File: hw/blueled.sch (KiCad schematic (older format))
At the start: 62 parts, among them J1 DC 5.5 - 42V, J2 LED Strip, J3 ICSP, J4 DC 5.5 - 42V, Q1 Q_PMOS_SDG, Q2 Q_PNP_EBC, Q3 BSS138, SW2 PUSH, U1 ATmega328P-AU, U2 HC-05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

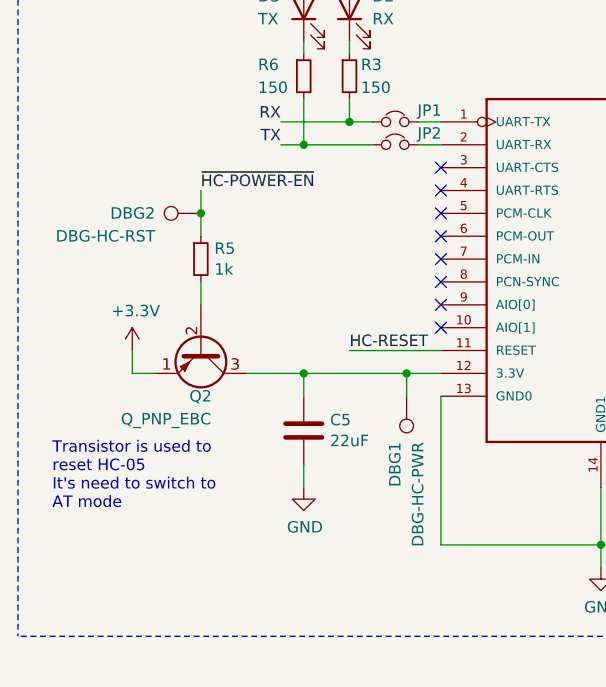
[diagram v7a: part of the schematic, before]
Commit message: fix(hw): change BJT to MOSFET to control HC-05 power
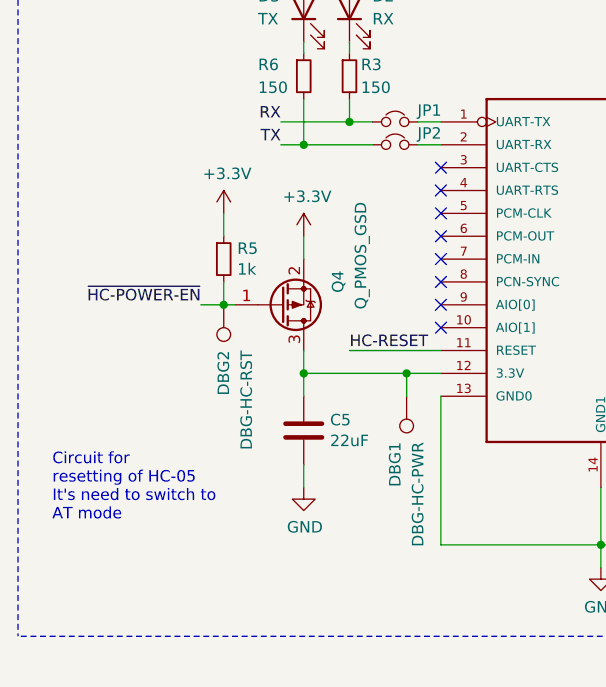
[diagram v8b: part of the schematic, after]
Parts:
- removed Q2: Q_PNP_EBC, Package_TO_SOT_SMD:SOT-323_SC-70_Handsoldering, symbol Device:Q_PNP_EBC
- added Q4: Q_PMOS_GSD, Package_TO_SOT_SMD:SOT-23, symbol Device:Q_PMOS_GSD
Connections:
- net +3V3: now also R5.1, Q4.2 (S)
- net ~HC-POWER-EN: now also R5.2, Q4.1 (G); no longer R5.1
- net at C5.1, DBG1.1, U2.12 (3.3V): now also Q4.3 (D)
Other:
- note added: "Circuit for\nresetting of HC-05\nIt's need to switch to \nAT mode"
- note removed: "Transistor is used to \nreset HC-05\nIt's need to switch to \nAT mode"
- moved on the sheet: DBG2, R5
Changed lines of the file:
@@
 Wire Wire Line
 	1850 5400 1850 5300
-Text Label 1400 4500 0    50   ~ 0
+Text Label 1400 5000 2    50   ~ 0
 ~HC-POWER-EN
 $Comp
 L Device:R_Small R5
 U 1 1 5E8E07EF
-P 1400 4800
-F 0 "R5" H 1459 4846 50  0000 L CNN
-F 1 "1k" H 1459 4755 50  0000 L CNN
-F 2 "Resistor_SMD:R_0805_2012Metric_Pad1.15x1.40mm_HandSolder" H 1400 4800 50  0001 C CNN
-F 3 "https://datasheet.lcsc.com/szlcsc/1810010118_YAGEO-RC0805FR-071KL_C95781.pdf" H 1400 4800 50  0001 C CNN
-F 4 "lcsc.com" H 1400 4800 50  0001 C CNN "Distributor"
-F 5 "RC0805FR-071KL" H 1400 4800 50  0001 C CNN "Manuf. Part"
-	1    1400 4800
-	1    0    0    -1
-$EndComp
-Wire Wire Line
-	1400 4500 1400 4600
-Wire Wire Line
-	1400 4900 1400 5000
-Wire Wire Line
-	1400 4600 1400 4700
-Connection ~ 1400 4600
+P 1500 4800
+F 0 "R5" H 1559 4846 50  0000 L CNN
+F 1 "1k" H 1559 4755 50  0000 L CNN
+F 2 "Resistor_SMD:R_0805_2012Metric_Pad1.15x1.40mm_HandSolder" H 1500 4800 50  0001 C CNN
+F 3 "https://datasheet.lcsc.com/szlcsc/1810010118_YAGEO-RC0805FR-071KL_C95781.pdf" H 1500 4800 50  0001 C CNN
+F 4 "lcsc.com" H 1500 4800 50  0001 C CNN "Distributor"
+F 5 "RC0805FR-071KL" H 1500 4800 50  0001 C CNN "Manuf. Part"
+	1    1500 4800
+	1    0    0    -1
+$EndComp
 $Comp
 L Connector:TestPoint DBG2
 U 1 1 5EAA6065
-P 1400 4600
-F 0 "DBG2" V 1400 4800 50  0000 L CNN
-F 1 "DBG-HC-RST" V 1300 4800 50  0000 L CNN
-F 2 "TestPoint:TestPoint_Pad_D1.0mm" H 1600 4600 50  0001 C CNN
-F 3 "~" H 1600 4600 50  0001 C CNN
-	1    1400 4600
-	0    -1   -1   0
-$EndComp
-$Comp
-L Device:Q_PNP_EBC Q2
-U 1 1 5E8AAEF6
-P 1400 5200
-F 0 "Q2" V 1600 5150 50  0000 L CNN
-F 1 "Q_PNP_EBC" V 1700 4850 50  0000 L CNN
-F 2 "Package_TO_SOT_SMD:SOT-323_SC-70_Handsoldering" H 1600 5300 50  0001 C CNN
-F 3 "https://datasheet.lcsc.com/szlcsc/1808280000_ROHM-Semicon-UMT2907A_C122972.pdf" H 1400 5200 50  0001 C CNN
-F 4 "lcsc.com" H 1400 5200 50  0001 C CNN "Distributor"
-F 5 "UMT2907A" H 1400 5200 50  0001 C CNN "Manuf. Part"
-	1    1400 5200
-	0    1    1    0
-$EndComp
-Wire Wire Line
-	1100 5300 1100 5200
-$Comp
-L power:+3.3V #PWR02
-U 1 1 5EB1E141
-P 1100 5200
-F 0 "#PWR02" H 1100 5050 50  0001 C CNN
-F 1 "+3.3V" H 1115 5373 50  0000 C CNN
-F 2 "" H 1100 5200 50  0001 C CNN
-F 3 "" H 1100 5200 50  0001 C CNN
-	1    1100 5200
-	1    0    0    -1
-$EndComp
-Wire Wire Line
-	1100 5300 1200 5300
-Wire Wire Line
-	1600 5300 1850 5300
+P 1500 5000
+F 0 "DBG2" V 1500 5200 50  0000 L CNN
+F 1 "DBG-HC-RST" V 1400 5200 50  0000 L CNN
+F 2 "TestPoint:TestPoint_Pad_D1.0mm" H 1700 5000 50  0001 C CNN
+F 3 "~" H 1700 5000 50  0001 C CNN
+	1    1500 5000
+	-1   0    0    1
+$EndComp
 $Comp
 L Diode:BAS40-04 D6
@@
 Wire Wire Line
 	1850 5300 2300 5300
-Text Notes 750  5900 0    50   ~ 0
-Transistor is used to \nreset HC-05\nIt's need to switch to \nAT mode
+Text Notes 750  5950 0    50   ~ 0
+Circuit for\nresetting of HC-05\nIt's need to switch to \nAT mode
 Text Notes 5350 3600 0    50   ~ 0
 XY2500F-B-5.08-3P \nfor LED strip\n
@@
 F 1 "BSS138" V 10230 3750 50  0000 C CNN
 F 2 "Package_TO_SOT_SMD:SOT-23" H 10090 3675 50  0001 L CIN
-F 3 "https://www.fairchildsemi.com/datasheets/BS/BSS138.pdf" H 9890 3750 50  0001 L CNN
+F 3 "https://datasheet.lcsc.com/szlcsc/AnBon-BSS138_C193019.pdf" H 9890 3750 50  0001 L CNN
 F 4 "lcsc.com" H 9890 3750 50  0001 C CNN "Distributor"
 F 5 "BSS138" H 9890 3750 50  0001 C CNN "Manuf. Part"
@@
 	1    0    0    -1
 $EndComp
+$Comp
+L Device:Q_PMOS_GSD Q4
+U 1 1 600573C9
+P 1750 5000
+F 0 "Q4" V 2000 4850 50  0000 L CNN
+F 1 "Q_PMOS_GSD" V 2100 4550 50  0000 L CNN
+F 2 "Package_TO_SOT_SMD:SOT-23" H 1950 5100 50  0001 C CNN
+F 3 "" H 1750 5000 50  0001 C CNN
+F 4 "lcsc.com" H 1750 5000 50  0001 C CNN "Distributor"
+F 5 "" H 1750 5000 50  0001 C CNN "Manuf. Part"
+	1    1750 5000
+	1    0    0    1
+$EndComp
+$Comp
+L power:+3.3V #PWR0113
+U 1 1 6008BB44
+P 1850 4700
+F 0 "#PWR0113" H 1850 4550 50  0001 C CNN
+F 1 "+3.3V" H 1865 4873 50  0000 C CNN
+F 2 "" H 1850 4700 50  0001 C CNN
+F 3 "" H 1850 4700 50  0001 C CNN
+	1    1850 4700
+	1    0    0    -1
+$EndComp
+Wire Wire Line
+	1850 4700 1850 4800
+Wire Wire Line
+	1850 5300 1850 5200
+Wire Wire Line
+	1550 5000 1500 5000
+Connection ~ 1500 5000
+Wire Wire Line
+	1500 5000 1400 5000
+Wire Wire Line
+	1500 5000 1500 4900
+$Comp
+L power:+3.3V #PWR0114
+U 1 1 60117B41
+P 1500 4600
+F 0 "#PWR0114" H 1500 4450 50  0001 C CNN
+F 1 "+3.3V" H 1515 4773 50  0000 C CNN
+F 2 "" H 1500 4600 50  0001 C CNN
+F 3 "" H 1500 4600 50  0001 C CNN
+	1    1500 4600
+	1    0    0    -1
+$EndComp
+Wire Wire Line
+	1500 4600 1500 4700
 $EndSCHEMATC
